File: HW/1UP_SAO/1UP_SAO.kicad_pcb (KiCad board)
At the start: 2 copper layers, 48 x 48 mm, 17 parts, among them X1 Badgelife_sao_connector_v169b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

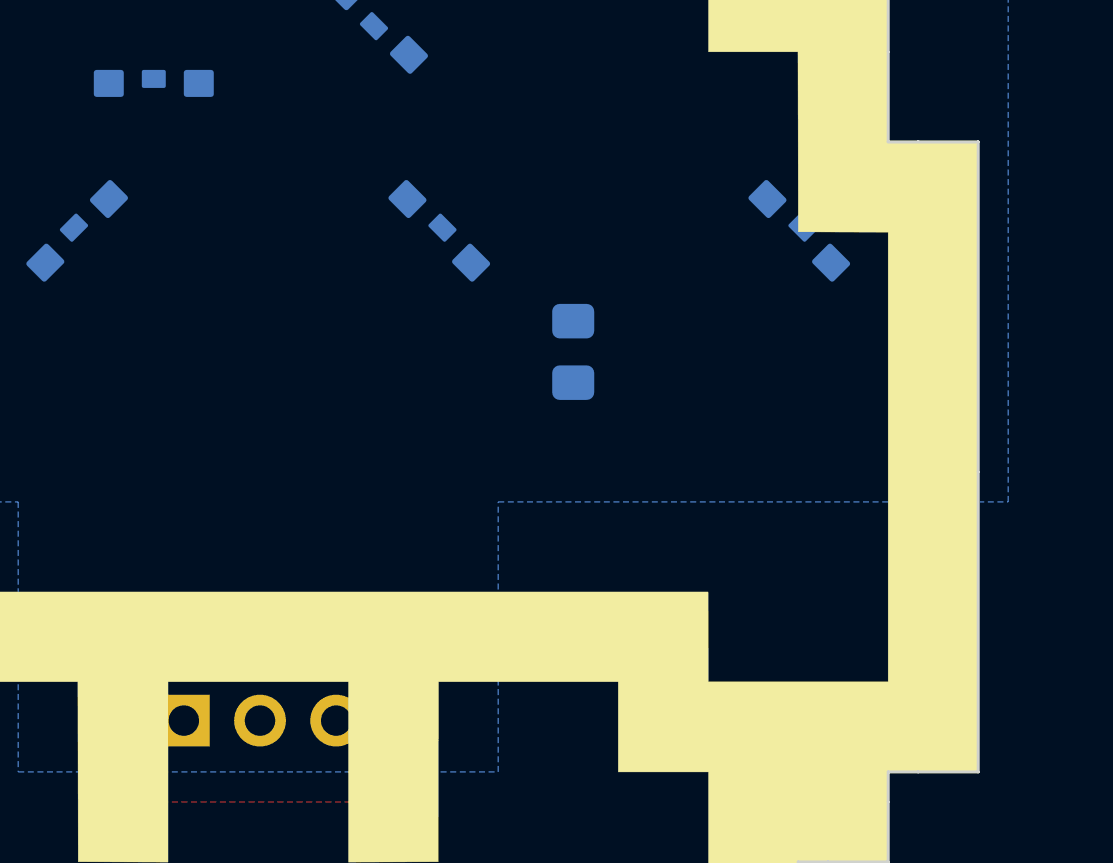
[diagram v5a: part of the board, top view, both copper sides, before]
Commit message: cleaning up and testing apature layers
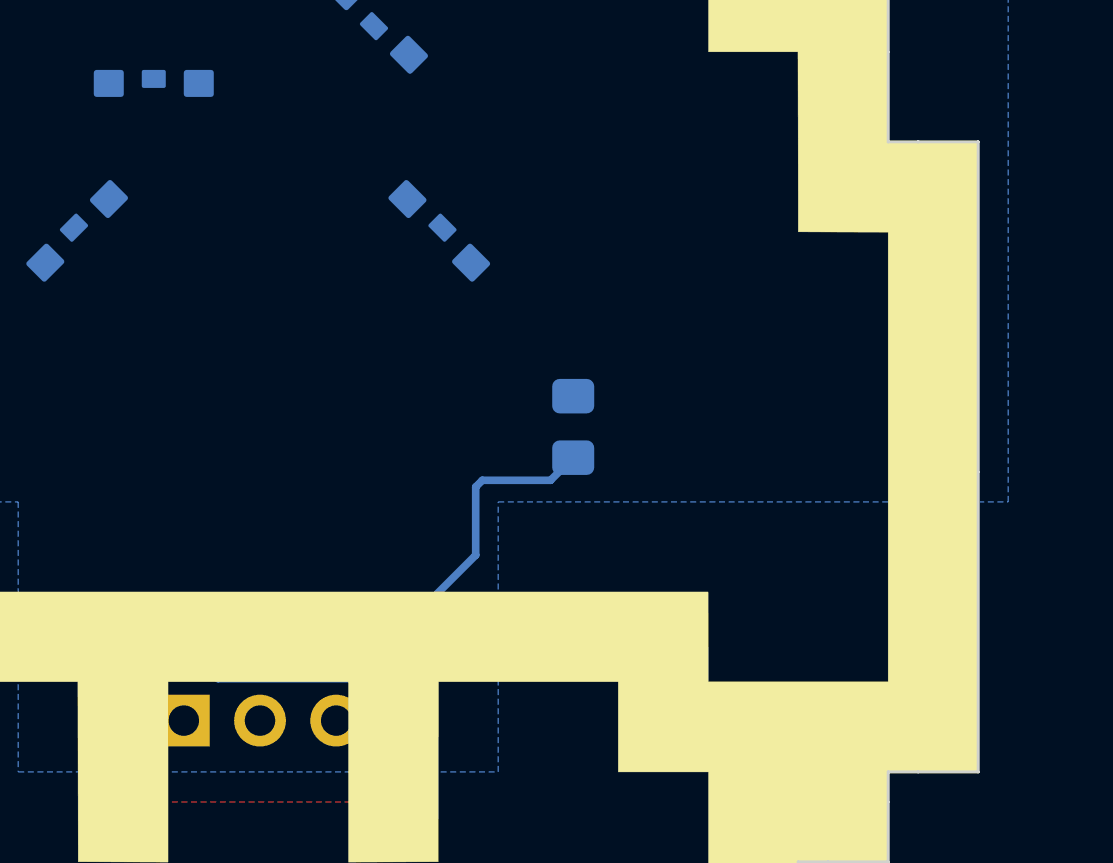
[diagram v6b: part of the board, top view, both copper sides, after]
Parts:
- moved D6 5.00 mm to (122.0, 97.0), turned to 270 degrees
- moved R2 2.50 mm to (110.5, 100.5)
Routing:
- net VCC: track 0.00 -> 17.8 mm
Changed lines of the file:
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@@
     (thickness 1.6)
     (drawings 66)
-    (tracks 0)
+    (tracks 7)
     (zones 0)
     (modules 17)
@@
     (36 B.SilkS user)
     (37 F.SilkS user hide)
-    (38 B.Mask user hide)
+    (38 B.Mask user)
     (39 F.Mask user hide)
     (40 Dwgs.User user hide)
@@
       (effects (font (size 1.524 1.524) (thickness 0.3)))
     )
-    (fp_poly (pts (xy 6.00075 -18.00225) (xy 12.0015 -17.991522) (xy 12.0015 -12.0015) (xy 6.011617 -12.0015)
-      (xy 6.006183 -13.499042) (xy 6.00075 -14.996584) (xy 4.503208 -15.002017) (xy 3.005666 -15.007451)
-      (xy 3.005666 -20.997334) (xy 5.989882 -20.997334) (xy 6.00075 -18.00225)) (layer B.Mask) (width 0.01))
-    (fp_poly (pts (xy -3.005667 -15.007451) (xy -4.503209 -15.002017) (xy -6.00075 -14.996584) (xy -6.011618 -12.0015)
-      (xy -12.0015 -12.0015) (xy -12.0015 -17.991522) (xy -6.00075 -18.00225) (xy -5.995317 -19.499792)
-      (xy -5.989883 -20.997334) (xy -3.005667 -20.997334) (xy -3.005667 -15.007451)) (layer B.Mask) (width 0.01))
-    (fp_poly (pts (xy 17.996885 -9.001125) (xy 18.00225 -6.00075) (xy 19.499791 -5.995317) (xy 20.997333 -5.989883)
-      (xy 20.997333 3.005666) (xy 15.007166 3.005666) (xy 15.007166 0) (xy 12.0015 0)
-      (xy 12.0015 -8.995834) (xy 15.007166 -8.995834) (xy 15.007166 -12.0015) (xy 16.499343 -12.0015)
-      (xy 17.991521 -12.001501) (xy 17.996885 -9.001125)) (layer B.Mask) (width 0.01))
-    (fp_poly (pts (xy -15.007167 -8.995834) (xy -12.0015 -8.995834) (xy -12.0015 0) (xy -15.007167 0)
-      (xy -15.007167 3.005666) (xy -20.997334 3.005666) (xy -20.997334 -5.989883) (xy -19.499792 -5.995317)
-      (xy -18.00225 -6.00075) (xy -17.991522 -12.0015) (xy -15.007167 -12.0015) (xy -15.007167 -8.995834)) (layer B.Mask) (width 0.01))
-    (fp_poly (pts (xy 6.00075 -6.00075) (xy 7.498291 -5.995317) (xy 8.995833 -5.989883) (xy 8.995833 1.989382)
-      (xy 7.498291 1.994816) (xy 6.00075 2.00025) (xy 5.995316 3.497791) (xy 5.989882 4.995333)
-      (xy -5.989883 4.995333) (xy -5.995317 3.497791) (xy -6.00075 2.00025) (xy -8.995834 1.989382)
-      (xy -8.995834 -5.989883) (xy -7.498292 -5.995317) (xy -6.00075 -6.00075) (xy -5.995317 -7.498292)
-      (xy -5.989883 -8.995834) (xy 5.989882 -8.995834) (xy 6.00075 -6.00075)) (layer B.Mask) (width 0.01))
+    (fp_poly (pts (xy 5.990166 -17.991667) (xy 12.0015 -17.991667) (xy 12.0015 -12.0015) (xy 6.011333 -12.0015)
+      (xy 6.011333 -15.007167) (xy 3.005666 -15.007167) (xy 3.005666 -20.997334) (xy 5.990166 -20.997334)
+      (xy 5.990166 -17.991667)) (layer B.Mask) (width 0.01))
+    (fp_poly (pts (xy -3.005667 -15.007167) (xy -6.011334 -15.007167) (xy -6.011334 -12.0015) (xy -12.0015 -12.0015)
+      (xy -12.0015 -17.991667) (xy -5.990167 -17.991667) (xy -5.990167 -20.997334) (xy -3.005667 -20.997334)
+      (xy -3.005667 -15.007167)) (layer B.Mask) (width 0.01))
+    (fp_poly (pts (xy -16.002 -8.001) (xy -13.0175 -8.001) (xy -13.0175 -1.016) (xy -16.002 -1.016)
+      (xy -16.002 1.989666) (xy -20.0025 1.989666) (xy -20.0025 -4.995334) (xy -16.996834 -4.995334)
+      (xy -16.996834 -10.9855) (xy -16.002 -10.9855) (xy -16.002 -8.001)) (layer B.Mask) (width 0.01))
+    (fp_poly (pts (xy 17.991666 -5.990167) (xy 20.997333 -5.990167) (xy 20.997333 2.9845) (xy 15.007166 2.9845)
+      (xy 15.007166 0) (xy 12.0015 0) (xy 12.0015 -8.995834) (xy 15.007166 -8.995834)
+      (xy 15.007166 -12.0015) (xy 17.991666 -12.0015) (xy 17.991666 -5.990167)) (layer B.Mask) (width 0.01))
+    (fp_poly (pts (xy 4.995333 -4.995334) (xy 8.001 -4.995334) (xy 8.001 1.989666) (xy 4.995333 1.989666)
+      (xy 4.995333 4.995333) (xy -4.995334 4.995333) (xy -4.995334 1.989666) (xy -8.001 1.989666)
+      (xy -8.001 -4.995334) (xy -4.995334 -4.995334) (xy -4.995334 -8.001) (xy 4.995333 -8.001)
+      (xy 4.995333 -4.995334)) (layer B.Mask) (width 0.01))
   )
   (module 1UP_SAO:Badgelife-SAOv169-SAO-2x3 (layer F.Cu)
@@
     (fp_line (start 0.3 -1.25) (end 0.3 -1.85) (layer B.SilkS) (width 0.15))
     (fp_arc (start 0 0.4) (end 1 0.4) (angle 180) (layer B.SilkS) (width 0.15))
-    (fp_text user "-    +" (at 0 -1 90 unlocked) (layer B.SilkS)
-      (effects (font (size 0.7 0.7) (thickness 0.15)) (justify mirror))
-    )
     (pad "" smd roundrect (at 0 -0.2 90) (size 0.8 0.6) (layers B.Cu B.Paste B.Mask) (roundrect_rratio 0.1))
     (pad 2 smd roundrect (at 1.5 -0.05 90) (size 1 0.9) (layers B.Cu B.Paste B.Mask) (roundrect_rratio 0.1)
@@
     (fp_line (start 0.3 -1.25) (end 0.3 -1.85) (layer B.SilkS) (width 0.15))
     (fp_arc (start 0 0.4) (end 1 0.4) (angle 180) (layer B.SilkS) (width 0.15))
-    (fp_text user "-    +" (at 0 -1 315 unlocked) (layer B.SilkS)
-      (effects (font (size 0.7 0.7) (thickness 0.15)) (justify mirror))
-    )
     (pad "" smd roundrect (at 0 -0.2 315) (size 0.8 0.6) (layers B.Cu B.Paste B.Mask) (roundrect_rratio 0.1))
     (pad 2 smd roundrect (at 1.5 -0.05 315) (size 1 0.9) (layers B.Cu B.Paste B.Mask) (roundrect_rratio 0.1)
@@
   )
   (module 1UP_SAO:1204_SIDE_VIEW_LED locked (layer B.Cu)
-    (at 118 94 315)
-    (fp_text reference D6 (at -3.1 0 225) (layer B.SilkS)
+    (at 122 97 270)
+    (fp_text reference D6 (at -3.1 0 180) (layer B.SilkS)
       (effects (font (size 0.7 0.7) (thickness 0.15)) (justify mirror))
     )
-    (fp_text value LED (at 0 4.199999 135) (layer B.Fab)
+    (fp_text value LED (at 0 4.199999 90) (layer B.Fab)
       (effects (font (size 1 1) (thickness 0.15)) (justify mirror))
     )
@@
     (fp_line (start 0.3 -1.25) (end 0.3 -1.85) (layer B.SilkS) (width 0.15))
     (fp_arc (start 0 0.4) (end 1 0.4) (angle 180) (layer B.SilkS) (width 0.15))
-    (pad "" smd roundrect (at 0 -0.2 315) (size 0.8 0.6) (layers B.Cu B.Paste B.Mask) (roundrect_rratio 0.1))
-    (pad 2 smd roundrect (at 1.5 -0.05 315) (size 1 0.9) (layers B.Cu B.Paste B.Mask) (roundrect_rratio 0.1)
+    (pad "" smd roundrect (at 0 -0.2 270) (size 0.8 0.6) (layers B.Cu B.Paste B.Mask) (roundrect_rratio 0.1))
+    (pad 2 smd roundrect (at 1.5 -0.05 270) (size 1 0.9) (layers B.Cu B.Paste B.Mask) (roundrect_rratio 0.1)
       (net 3 "Net-(D5-Pad2)"))
-    (pad 1 smd roundrect (at -1.5 -0.05 315) (size 1 0.9) (layers B.Cu B.Paste B.Mask) (roundrect_rratio 0.1)
+    (pad 1 smd roundrect (at -1.5 -0.05 270) (size 1 0.9) (layers B.Cu B.Paste B.Mask) (roundrect_rratio 0.1)
       (net 2 GND))
   )
@@
   )
   (module Resistor_SMD:R_0805_2012Metric_Pad1.15x1.40mm_HandSolder locked (layer B.Cu)
-    (at 110.5 98 90)
+    (at 110.5 100.5 90)
     (descr "Resistor SMD 0805 (2012 Metric), square (rectangular) end terminal, IPC_7351 nominal with elongated pad for handsoldering. (Body size source: https://docs.google.com/spreadsheets/d/1BsfQQcO9C6DZCsRaXUlFlo91Tg2WpOkGARC1WS5S8t0/edit?usp=sharing), generated with kicad-footprint-generator")
     (tags "resistor handsolder")
@@
   (gr_line (start 85 124) (end 85 123) (layer Edge.Cuts) (width 0.1))
   (gr_line (start 85 123) (end 85 123) (layer Edge.Cuts) (width 0.1))
+  (segment (start 109.74559 102.27941) (end 110.5 101.525) (width 0.254) (layer B.Cu) (net 8))
+  (segment (start 107.47059 102.27941) (end 109.74559 102.27941) (width 0.254) (layer B.Cu) (net 8))
+  (segment (start 97.52 107.75) (end 98.663001 108.893001) (width 0.254) (layer B.Cu) (net 8))
+  (segment (start 107.25 102.5) (end 107.47059 102.27941) (width 0.254) (layer B.Cu) (net 8))
+  (segment (start 98.663001 108.893001) (end 103.131999 108.893001) (width 0.254) (layer B.Cu) (net 8))
+  (segment (start 103.131999 108.893001) (end 107.25 104.775) (width 0.254) (layer B.Cu) (net 8))
+  (segment (start 107.25 104.775) (end 107.25 102.5) (width 0.254) (layer B.Cu) (net 8))
   (zone (net 2) (net_name GND) (layer B.Cu) (hatch edge 0.508)
     (connect_pads (clearance 0))
@@
     (polygon
       (pts
-        (xy 106 91) (xy 94 91) (xy 94 94) (xy 91 94) (xy 91 102)
-        (xy 94 102) (xy 94 105) (xy 106 105) (xy 106 102) (xy 109 102)
-        (xy 109 94) (xy 106 94)
+        (xy 105 92) (xy 95 92) (xy 95 95) (xy 92 95) (xy 92 102)
+        (xy 95 102) (xy 95 105) (xy 105 105) (xy 105 102) (xy 108 102)
+        (xy 108 95) (xy 105 95)
       )
     )

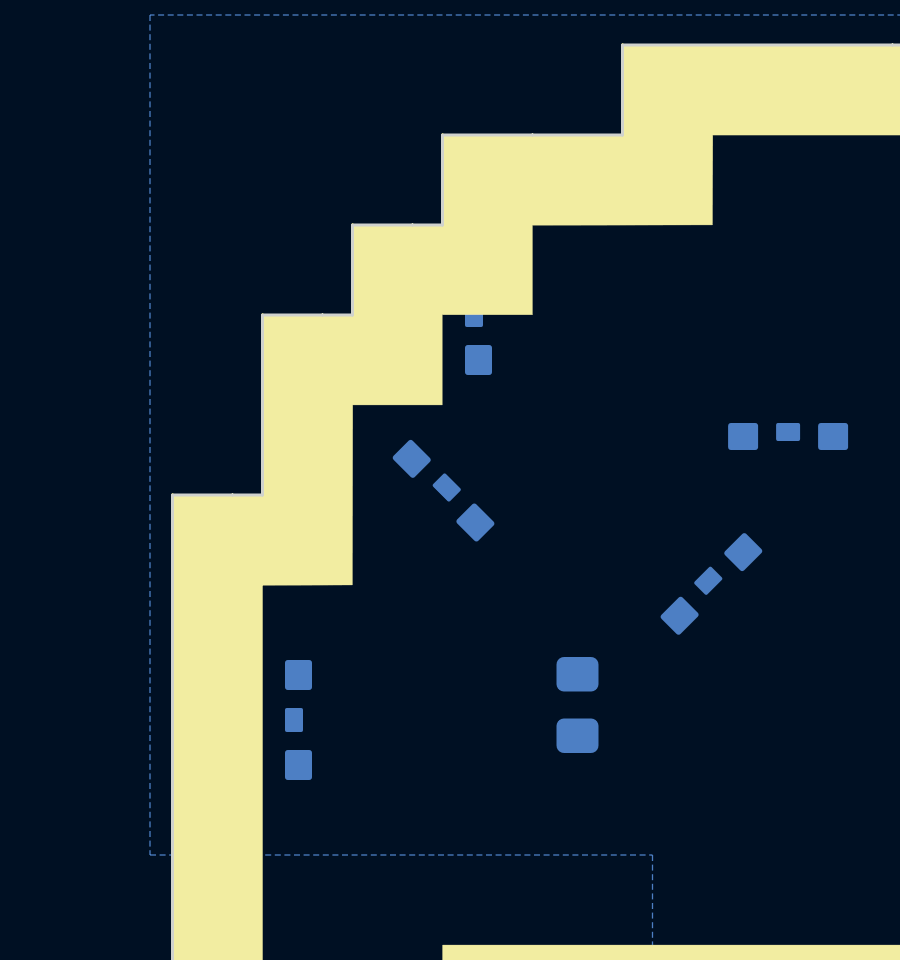
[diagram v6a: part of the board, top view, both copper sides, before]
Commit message: shrinking b.mask, updating keepouts, LED placement
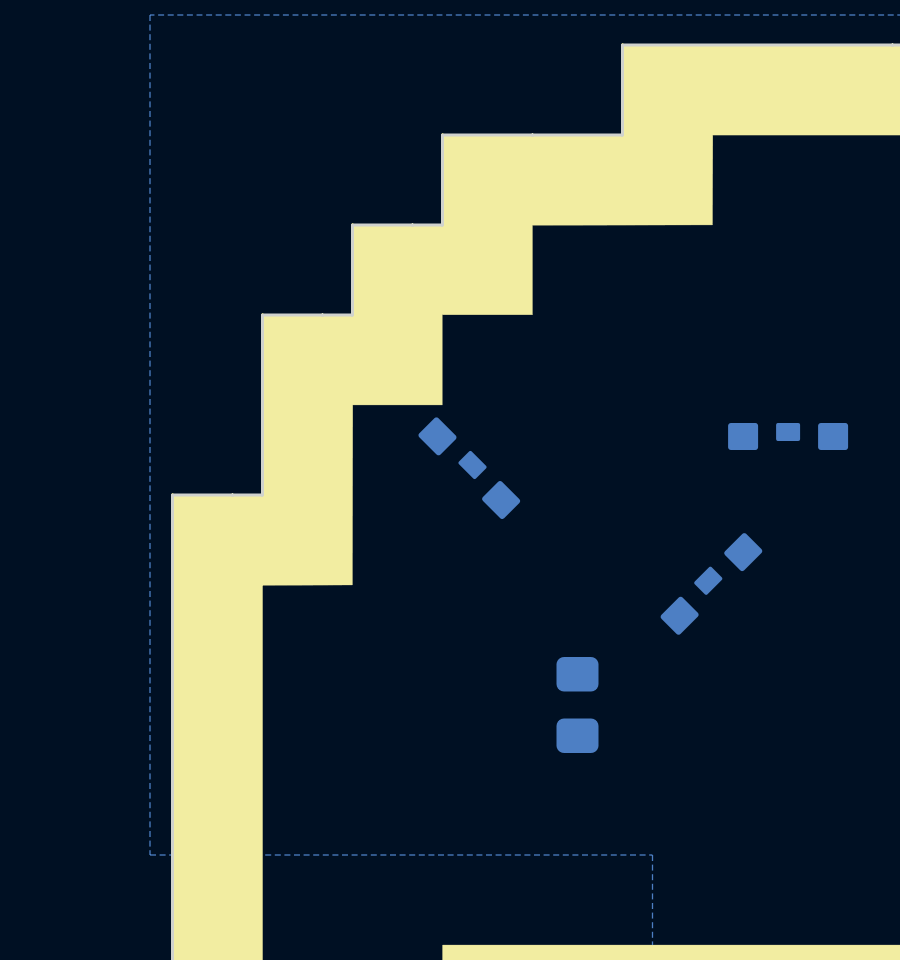
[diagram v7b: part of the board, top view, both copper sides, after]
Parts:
- moved D1 6.21 mm to (91.0, 81.0), turned to 0 degrees
- moved D4 2.25 mm to (78.0, 98.5)
- moved D3 1.14 mm to (85.9, 90.1)
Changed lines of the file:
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@@
       (effects (font (size 1.524 1.524) (thickness 0.3)))
     )
-    (fp_poly (pts (xy 5.990166 -17.991667) (xy 12.0015 -17.991667) (xy 12.0015 -12.0015) (xy 6.011333 -12.0015)
-      (xy 6.011333 -15.007167) (xy 3.005666 -15.007167) (xy 3.005666 -20.997334) (xy 5.990166 -20.997334)
-      (xy 5.990166 -17.991667)) (layer B.Mask) (width 0.01))
+    (fp_poly (pts (xy 5.98176 -18.997084) (xy 5.966637 -16.996834) (xy 11.980333 -16.996834) (xy 11.980333 -12.0015)
+      (xy 6.011333 -12.0015) (xy 6.011333 -15.007167) (xy 3.005666 -15.007167) (xy 3.005666 -20.997334)
+      (xy 5.996884 -20.997334) (xy 5.98176 -18.997084)) (layer B.Mask) (width 0.01))
     (fp_poly (pts (xy -3.005667 -15.007167) (xy -6.011334 -15.007167) (xy -6.011334 -12.0015) (xy -12.0015 -12.0015)
-      (xy -12.0015 -17.991667) (xy -5.990167 -17.991667) (xy -5.990167 -20.997334) (xy -3.005667 -20.997334)
+      (xy -12.0015 -16.996834) (xy -5.990167 -16.996834) (xy -5.990167 -20.997334) (xy -3.005667 -20.997334)
       (xy -3.005667 -15.007167)) (layer B.Mask) (width 0.01))
+    (fp_poly (pts (xy 17.991666 -4.995334) (xy 20.0025 -4.995334) (xy 20.0025 1.989666) (xy 16.002 1.989666)
+      (xy 16.002 -1.016) (xy 13.0175 -1.016) (xy 13.0175 -8.001) (xy 16.002 -8.001)
+      (xy 16.002 -10.9855) (xy 17.991666 -10.9855) (xy 17.991666 -4.995334)) (layer B.Mask) (width 0.01))
     (fp_poly (pts (xy -16.002 -8.001) (xy -13.0175 -8.001) (xy -13.0175 -1.016) (xy -16.002 -1.016)
-      (xy -16.002 1.989666) (xy -20.0025 1.989666) (xy -20.0025 -4.995334) (xy -16.996834 -4.995334)
-      (xy -16.996834 -10.9855) (xy -16.002 -10.9855) (xy -16.002 -8.001)) (layer B.Mask) (width 0.01))
-    (fp_poly (pts (xy 17.991666 -5.990167) (xy 20.997333 -5.990167) (xy 20.997333 2.9845) (xy 15.007166 2.9845)
-      (xy 15.007166 0) (xy 12.0015 0) (xy 12.0015 -8.995834) (xy 15.007166 -8.995834)
-      (xy 15.007166 -12.0015) (xy 17.991666 -12.0015) (xy 17.991666 -5.990167)) (layer B.Mask) (width 0.01))
+      (xy -16.002 1.989666) (xy -20.0025 1.989666) (xy -20.0025 -4.995334) (xy -17.991667 -4.995334)
+      (xy -17.991667 -10.9855) (xy -16.002 -10.9855) (xy -16.002 -8.001)) (layer B.Mask) (width 0.01))
     (fp_poly (pts (xy 4.995333 -4.995334) (xy 8.001 -4.995334) (xy 8.001 1.989666) (xy 4.995333 1.989666)
       (xy 4.995333 4.995333) (xy -4.995334 4.995333) (xy -4.995334 1.989666) (xy -8.001 1.989666)
@@
   )
   (module 1UP_SAO:1204_SIDE_VIEW_LED (layer B.Cu)
-    (at 80.25 98.5 90)
+    (at 78 98.5 90)
     (fp_text reference D4 (at -3.1 0 180) (layer B.SilkS)
       (effects (font (size 0.7 0.7) (thickness 0.15)) (justify mirror))
@@
     (fp_line (start 0.3 -1.25) (end 0.3 -1.85) (layer B.SilkS) (width 0.15))
     (fp_arc (start 0 0.4) (end 1 0.4) (angle 180) (layer B.SilkS) (width 0.15))
-    (fp_text user "-    +" (at 0 -1 45 unlocked) (layer B.SilkS)
-      (effects (font (size 0.7 0.7) (thickness 0.15)) (justify mirror))
-    )
     (pad "" smd roundrect (at 0 -0.2 45) (size 0.8 0.6) (layers B.Cu B.Paste B.Mask) (roundrect_rratio 0.1))
     (pad 2 smd roundrect (at 1.5 -0.05 45) (size 1 0.9) (layers B.Cu B.Paste B.Mask) (roundrect_rratio 0.1)
@@
     (fp_line (start 0.3 -1.25) (end 0.3 -1.85) (layer B.SilkS) (width 0.15))
     (fp_arc (start 0 0.4) (end 1 0.4) (angle 180) (layer B.SilkS) (width 0.15))
-    (fp_text user "-    +" (at 0 -1 315 unlocked) (layer B.SilkS)
-      (effects (font (size 0.7 0.7) (thickness 0.15)) (justify mirror))
-    )
     (pad "" smd roundrect (at 0 -0.2 315) (size 0.8 0.6) (layers B.Cu B.Paste B.Mask) (roundrect_rratio 0.1))
     (pad 2 smd roundrect (at 1.5 -0.05 315) (size 1 0.9) (layers B.Cu B.Paste B.Mask) (roundrect_rratio 0.1)
@@
     (fp_line (start 0.3 -1.25) (end 0.3 -1.85) (layer B.SilkS) (width 0.15))
     (fp_arc (start 0 0.4) (end 1 0.4) (angle 180) (layer B.SilkS) (width 0.15))
-    (fp_text user "-    +" (at 0.712764 -4.072935 135 unlocked) (layer B.SilkS)
-      (effects (font (size 0.7 0.7) (thickness 0.15)) (justify mirror))
-    )
     (pad "" smd roundrect (at 0 -0.2 135) (size 0.8 0.6) (layers B.Cu B.Paste B.Mask) (roundrect_rratio 0.1))
     (pad 2 smd roundrect (at 1.5 -0.05 135) (size 1 0.9) (layers B.Cu B.Paste B.Mask) (roundrect_rratio 0.1)
@@
   )
   (module 1UP_SAO:1204_SIDE_VIEW_LED (layer B.Cu)
-    (at 86.25 85 90)
-    (fp_text reference D1 (at -3.1 0 180) (layer B.SilkS)
+    (at 91 81)
+    (fp_text reference D1 (at -3.1 0 270) (layer B.SilkS)
       (effects (font (size 0.7 0.7) (thickness 0.15)) (justify mirror))
     )
-    (fp_text value LED (at 0 4.199999 90) (layer B.Fab)
+    (fp_text value LED (at 0 4.199999) (layer B.Fab)
       (effects (font (size 1 1) (thickness 0.15)) (justify mirror))
     )
@@
     (fp_line (start 0.3 -1.25) (end 0.3 -1.85) (layer B.SilkS) (width 0.15))
     (fp_arc (start 0 0.4) (end 1 0.4) (angle 180) (layer B.SilkS) (width 0.15))
-    (pad "" smd roundrect (at 0 -0.2 90) (size 0.8 0.6) (layers B.Cu B.Paste B.Mask) (roundrect_rratio 0.1))
-    (pad 2 smd roundrect (at 1.5 -0.05 90) (size 1 0.9) (layers B.Cu B.Paste B.Mask) (roundrect_rratio 0.1)
+    (pad "" smd roundrect (at 0 -0.2) (size 0.8 0.6) (layers B.Cu B.Paste B.Mask) (roundrect_rratio 0.1))
+    (pad 2 smd roundrect (at 1.5 -0.05) (size 1 0.9) (layers B.Cu B.Paste B.Mask) (roundrect_rratio 0.1)
       (net 1 "Net-(D1-Pad2)"))
-    (pad 1 smd roundrect (at -1.5 -0.05 90) (size 1 0.9) (layers B.Cu B.Paste B.Mask) (roundrect_rratio 0.1)
+    (pad 1 smd roundrect (at -1.5 -0.05) (size 1 0.9) (layers B.Cu B.Paste B.Mask) (roundrect_rratio 0.1)
       (net 2 GND))
   )
   (module 1UP_SAO:1204_SIDE_VIEW_LED (layer B.Cu)
-    (at 85 90.891421 315)
+    (at 85.858579 90.141421 315)
     (fp_text reference D3 (at -3.1 0 225) (layer B.SilkS)
       (effects (font (size 0.7 0.7) (thickness 0.15)) (justify mirror))
@@
     (polygon
       (pts
-        (xy 103 79) (xy 106 79) (xy 106 82) (xy 112 82) (xy 112 88)
+        (xy 103 79) (xy 106 79) (xy 106 83) (xy 112 83) (xy 112 88)
         (xy 106 88) (xy 106 85) (xy 103 85)
       )
@@
     (polygon
       (pts
-        (xy 97 79) (xy 94 79) (xy 94 82) (xy 88 82) (xy 88 88)
+        (xy 97 79) (xy 94 79) (xy 94 83) (xy 88 83) (xy 88 88)
         (xy 94 88) (xy 94 85) (xy 97 85)
       )
@@
     (polygon
       (pts
-        (xy 85 88) (xy 82 88) (xy 82 94) (xy 79 94) (xy 79 103)
-        (xy 85 103) (xy 85 100) (xy 88 100) (xy 88 91) (xy 85 91)
+        (xy 84 89) (xy 82 89) (xy 82 95) (xy 80 95) (xy 80 102)
+        (xy 84 102) (xy 84 99) (xy 87 99) (xy 87 92) (xy 84 92)
       )
     )
